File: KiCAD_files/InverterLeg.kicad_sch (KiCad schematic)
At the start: 76 parts, among them Q699 DMP3099L-7, U601 AMC1100DUB, U603 UCC21222DR, U605 ACS730KLCTR-20AB

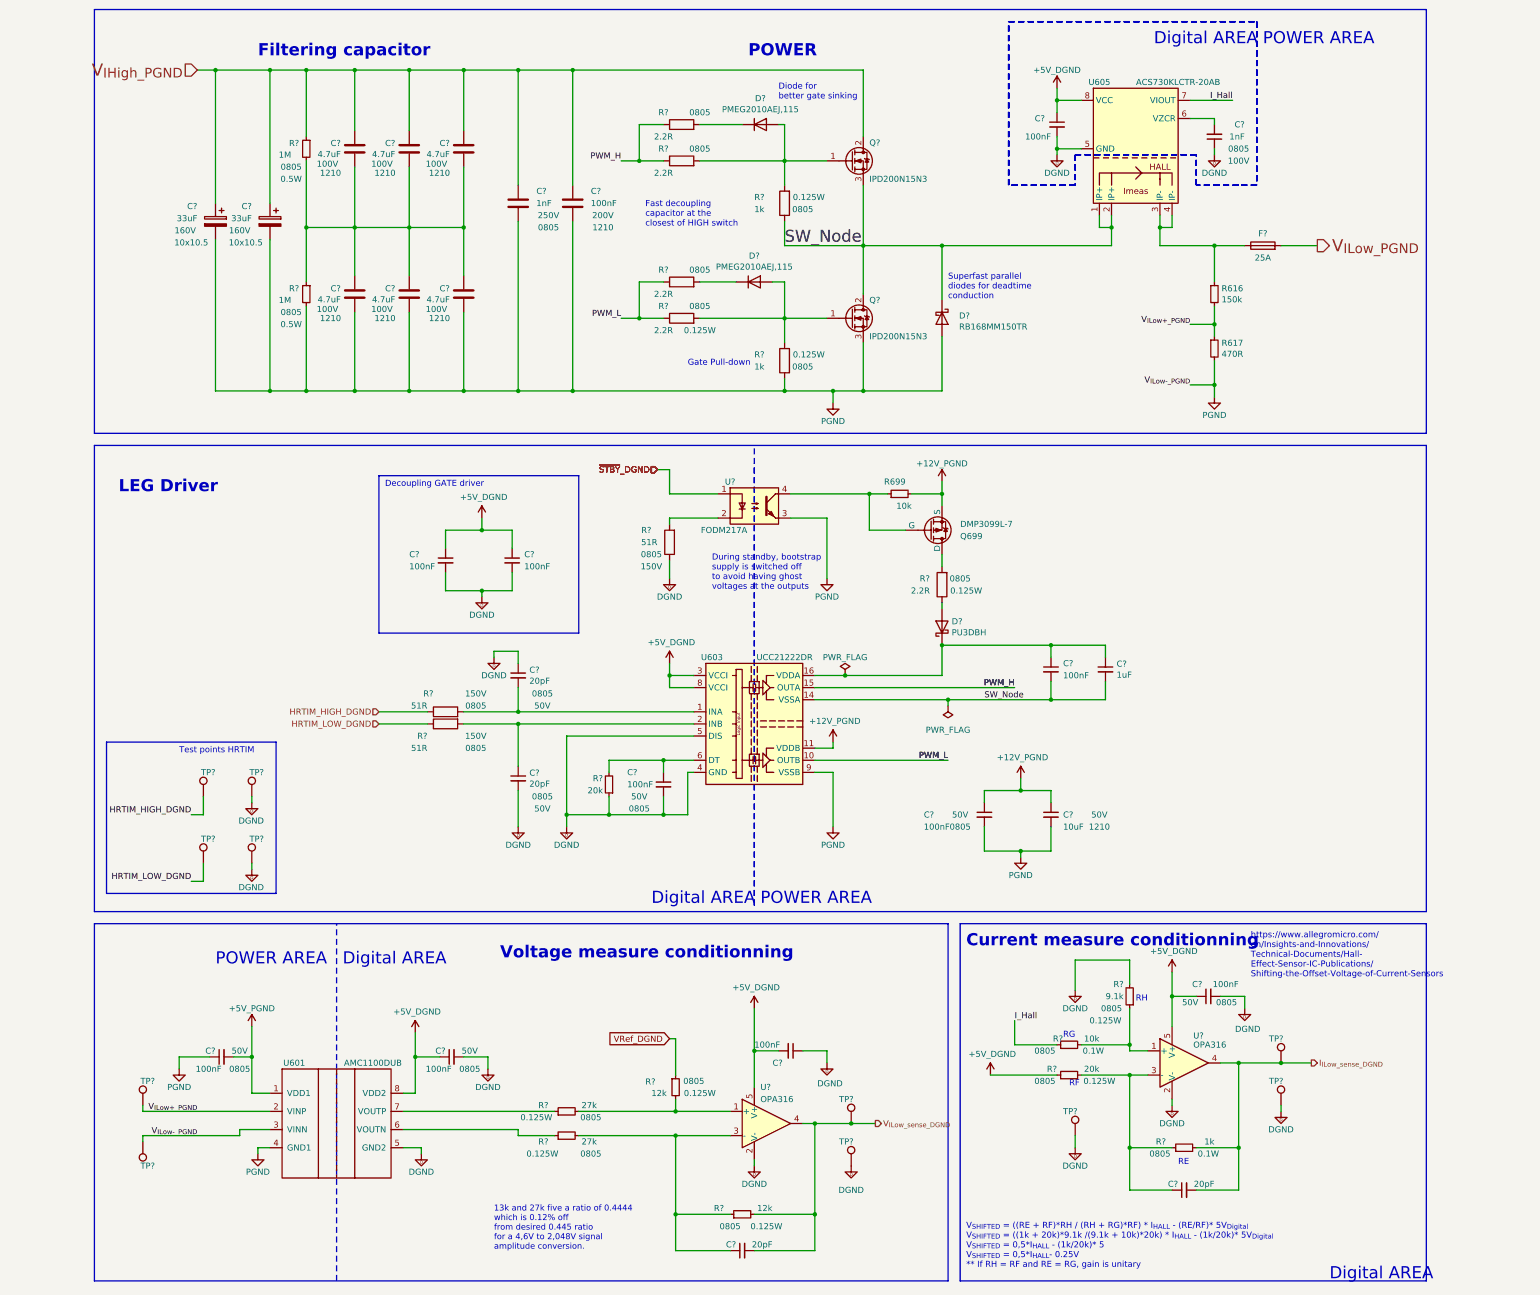
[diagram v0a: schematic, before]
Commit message: Added netclasses and ERC rules for isolation clearances
Signed-off-by: Jean Alinei <jean.alinei@laas.fr>
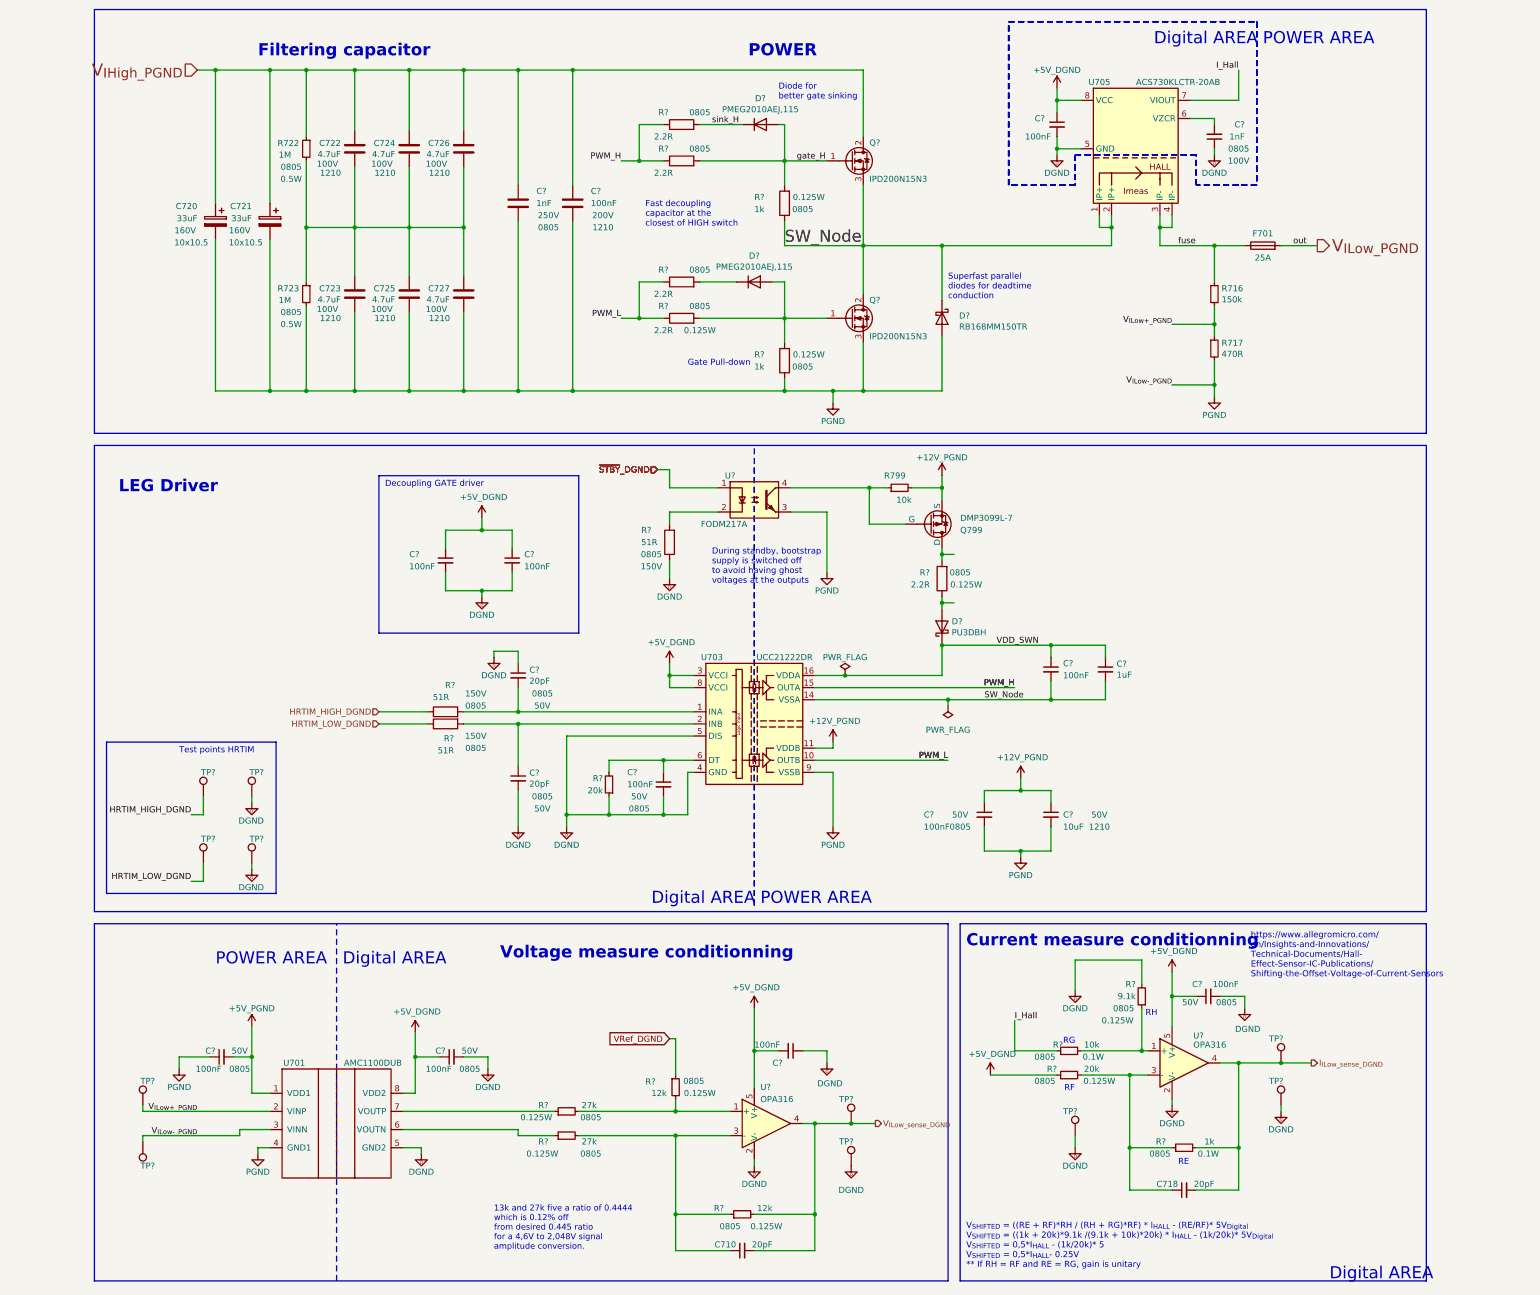
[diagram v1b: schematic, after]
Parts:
- gave numbers to parts that had none: 13
- renumbered Q699 to Q799, R616 to R716, R617 to R717, R699 to R799, U601 to U701, U603 to U703, U605 to U705
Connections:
- net VDD_SWN: now reaches C?.1, C?.1, D?.1 (K), U703.16 (VDDA)
- net sink_H: now reaches D?.1 (K), R?.2
- net gate_H: now reaches D?.2 (A), Q?.1 (G), R?.2, R?.2
- net fuse: now reaches F701.1, R716.1, U705.3 (IP-), U705.4 (IP-)
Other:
- moved on the sheet: Q799, R799, R?, U?
